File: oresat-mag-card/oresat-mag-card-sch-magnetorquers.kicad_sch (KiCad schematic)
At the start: 79 parts, among them U12 STSPIN250, U13 STSPIN250, U14 INA185, U15 INA185, U16 STSPIN250, U17 INA185

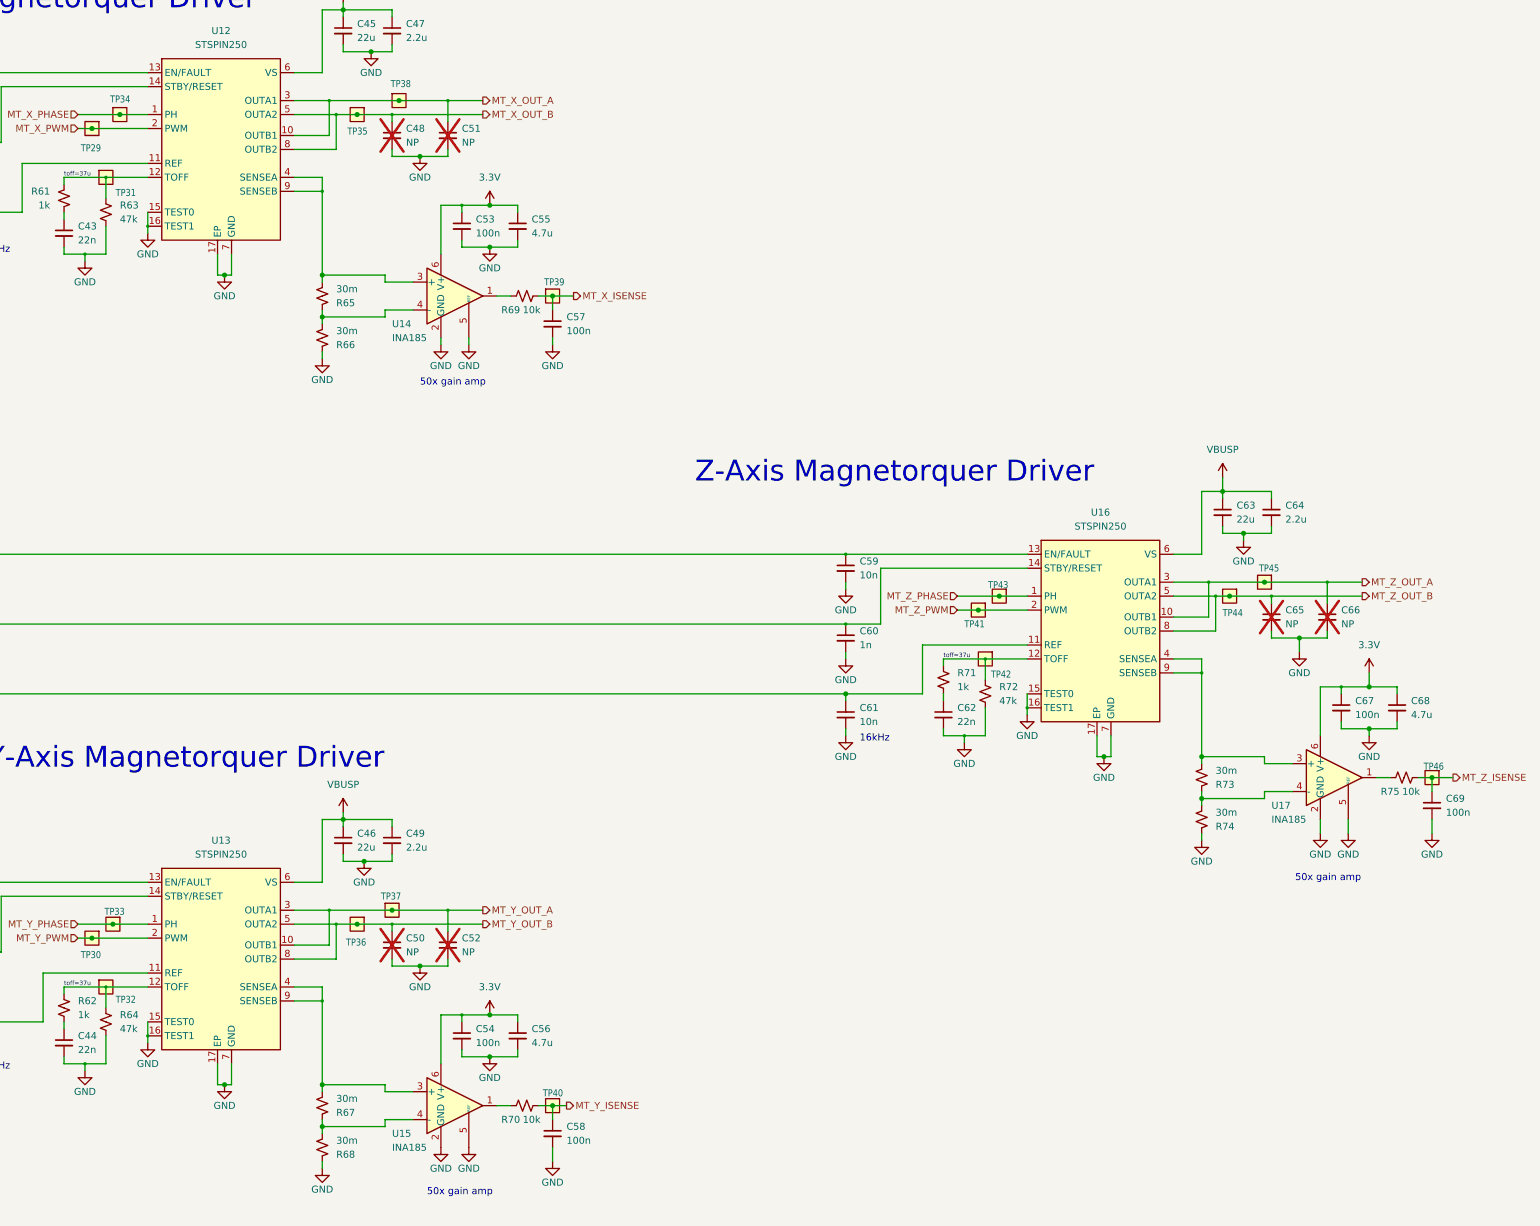
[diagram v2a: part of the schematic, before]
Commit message: Moved to independent MT connectors using pico EZ connectors, and re-laid out the STSPIN250s to be more best-practices.
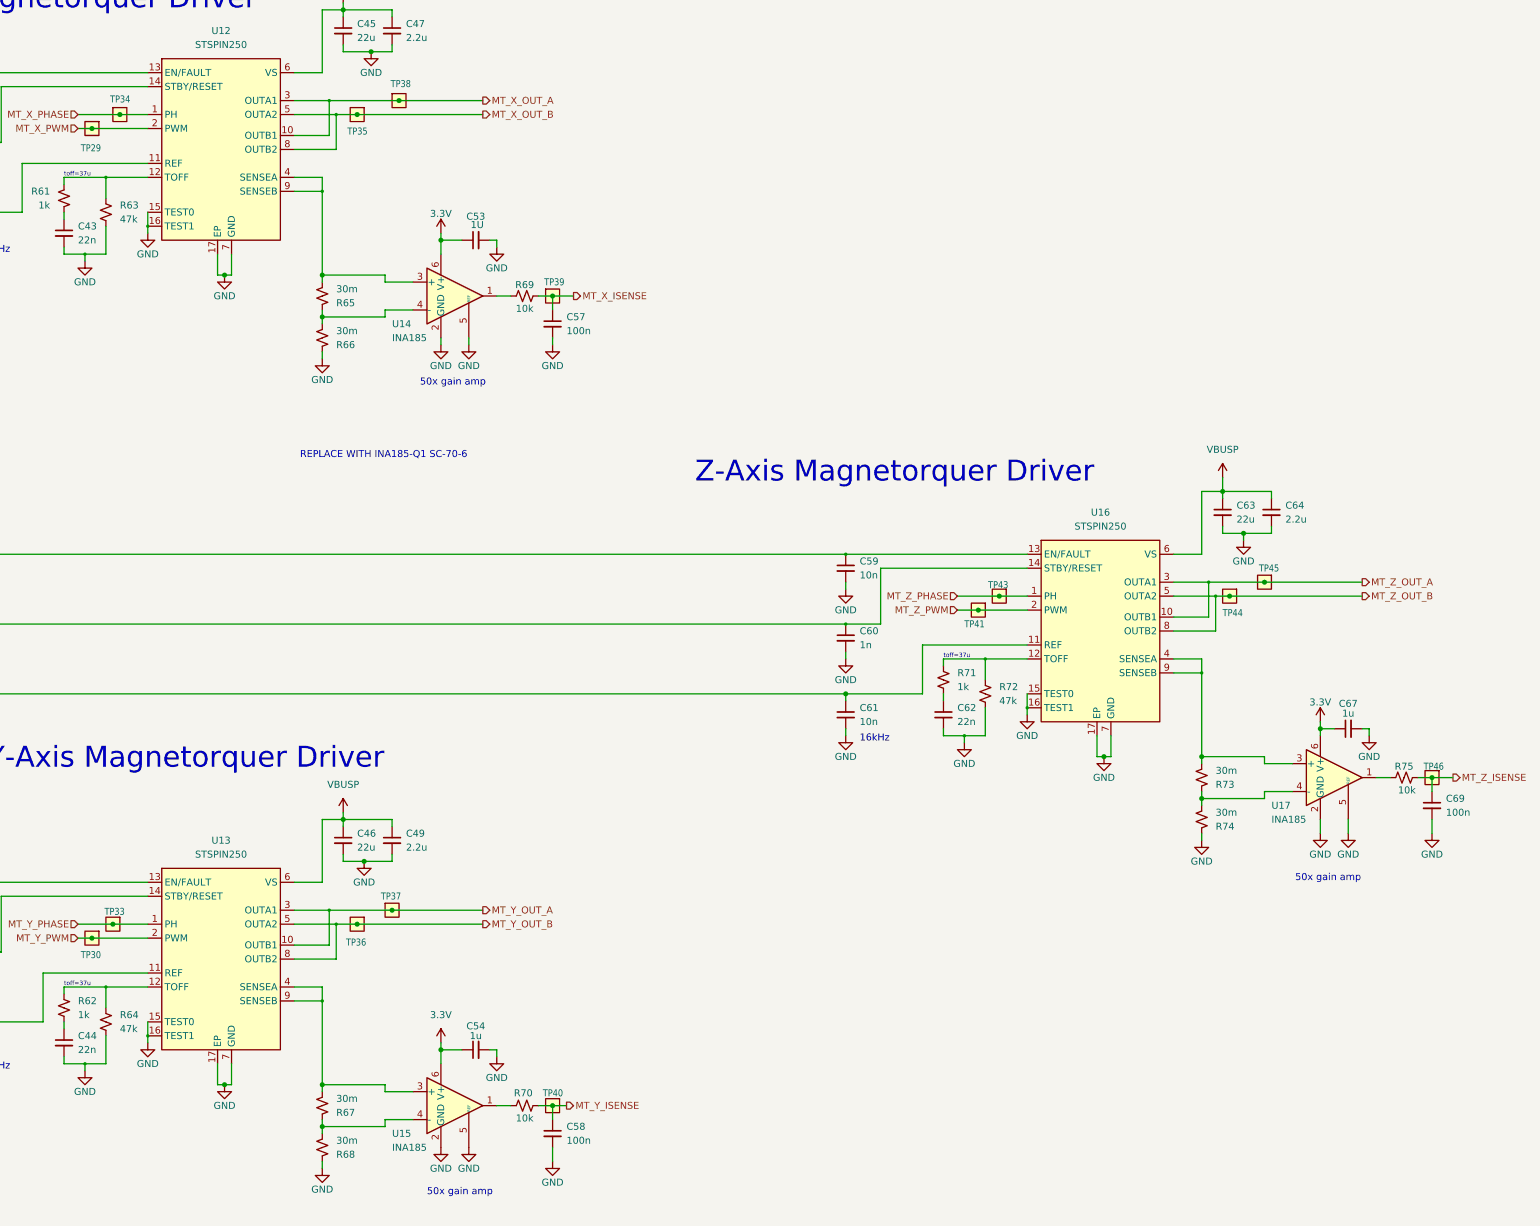
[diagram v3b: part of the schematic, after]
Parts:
- removed C48, C50, C51, C52, C65, C66: NP, oresat-passives:0603-C-NOSILK, symbol Device:C_Small
- removed C55, C56, C68: 4.7u, oresat-passives:0603-C-NOSILK, symbol Device:C_Small
- removed TP31, TP32, TP42: Test-Point, oresat-misc:TestPoint-0.75mm-th, symbol oresat-misc:Test-Point-0.75mm-th
- C37, C39, C40, C42, C59, C61: DIST (none) -> DigiKey; DPN (none) -> 399-12983-1-ND; MFR (none) -> KEMET; MPN (none) -> C0603C103J5RACAUTO
- C38, C41, C60: DIST (none) -> DigiKey; DPN (none) -> 399-12989-1-ND; MFR (none) -> KEMET; MPN (none) -> C0603C102J5RACAUTO
- C47, C49, C64: DIST (none) -> DigiKey; DPN (none) -> 490-GRT188C71E225KE13DCT-ND; MFR (none) -> Murata Electronics; MPN (none) -> GRT188C71E225KE13D
- C53: value 100n -> 1U; DIST (none) -> DigiKey; MFR (none) -> KEMET
- C54, C67: value 100n -> 1u; DIST (none) -> DigiKey; MFR (none) -> KEMET
- C57, C58, C69: DIST (none) -> DigiKey; DPN (none) -> 399-6856-1-ND; MFR (none) -> KEMET; MPN (none) -> C0603C104K5RACAUTO
- R57, R69, R70, R75: DIST (none) -> DigiKey; DPN (none) -> RMCF0603FT10K0CT-ND; MFR (none) -> Stackpole Electronics; MPN (none) -> RMCF0603FT10K0
- R59, R61, R62, R71: DIST (none) -> DigiKey; DPN (none) -> RMCF0603FT2K70CT-ND; MFR (none) -> Stackpole Electronics; MPN (none) -> RMCF0603FT1K00
- R63, R64, R72: DIST (none) -> DigiKey; DPN (none) -> RMCF0603FT47K0CT-ND; MFR (none) -> Stackpole Electronics; MPN (none) -> RMCF0603FT47K0
- R65, R66, R67, R68, R73, R74: DIST (none) -> DigiKey; DPN (none) -> CSR1206FK30L0CT-ND; MFR (none) -> Stackpole Electronics; MPN (none) -> CSR1206FK30L0
- U12, U13, U16: DIST (none) -> DigiKey; DPN (none) -> 497-17035-1-ND; MFR (none) -> STMicroelectronics; MPN (none) -> STSPIN250
- U14, U15, U17: DIST (none) -> DigiKey; DPN (none) -> 296-INA185A2QDCKRQ1CT-ND; MFR (none) -> Texas Instruments; MPN (none) -> INA185A2QDCKRQ1
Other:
- note added: "REPLACE WITH INA185-Q1 SC-70-6"
- moved on the sheet: C53, C54, C67

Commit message: Final mag card
Lots of polishing around best practices layout. Put in giant hole to thread the MTs from below if required for the 3U CubeSats. Cleaned up power layer, added stitching vias, updated readme.
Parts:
- C37, C38, C39, C40, C41, C42, C47, C49, C53, C54, C57, C58, C59, C60, C61, C64, C67, C69, R57, R59, R61, R62, R63, R64, R65, R66, R67, R68, R69, R70, R71, R72, R73, R74, R75, U12, U13, U14, U15, U16, U17: DIS (none) -> DigiKey; DIST DigiKey -> (none)
- C45, C46, C63: DIS (none) -> DigiKey

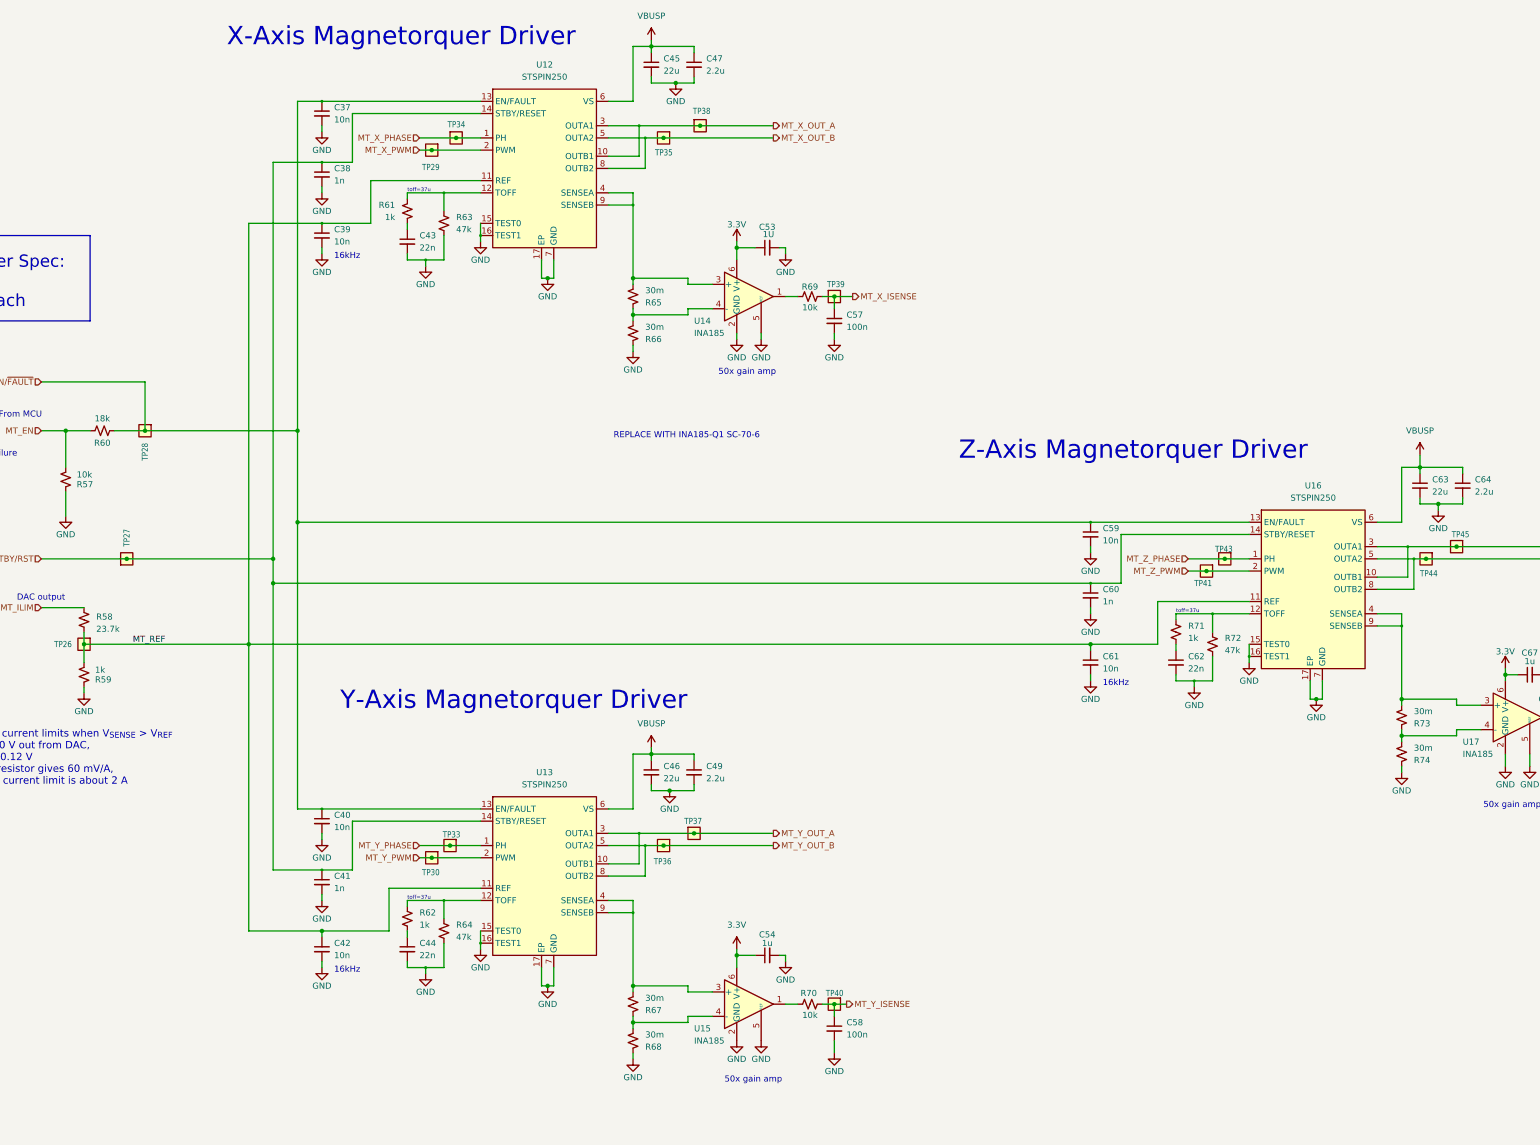
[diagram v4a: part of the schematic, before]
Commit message: Upgraded to kiCad 10, updated BOM during fabrication woes with Colorodo PCBA, no change in PCB
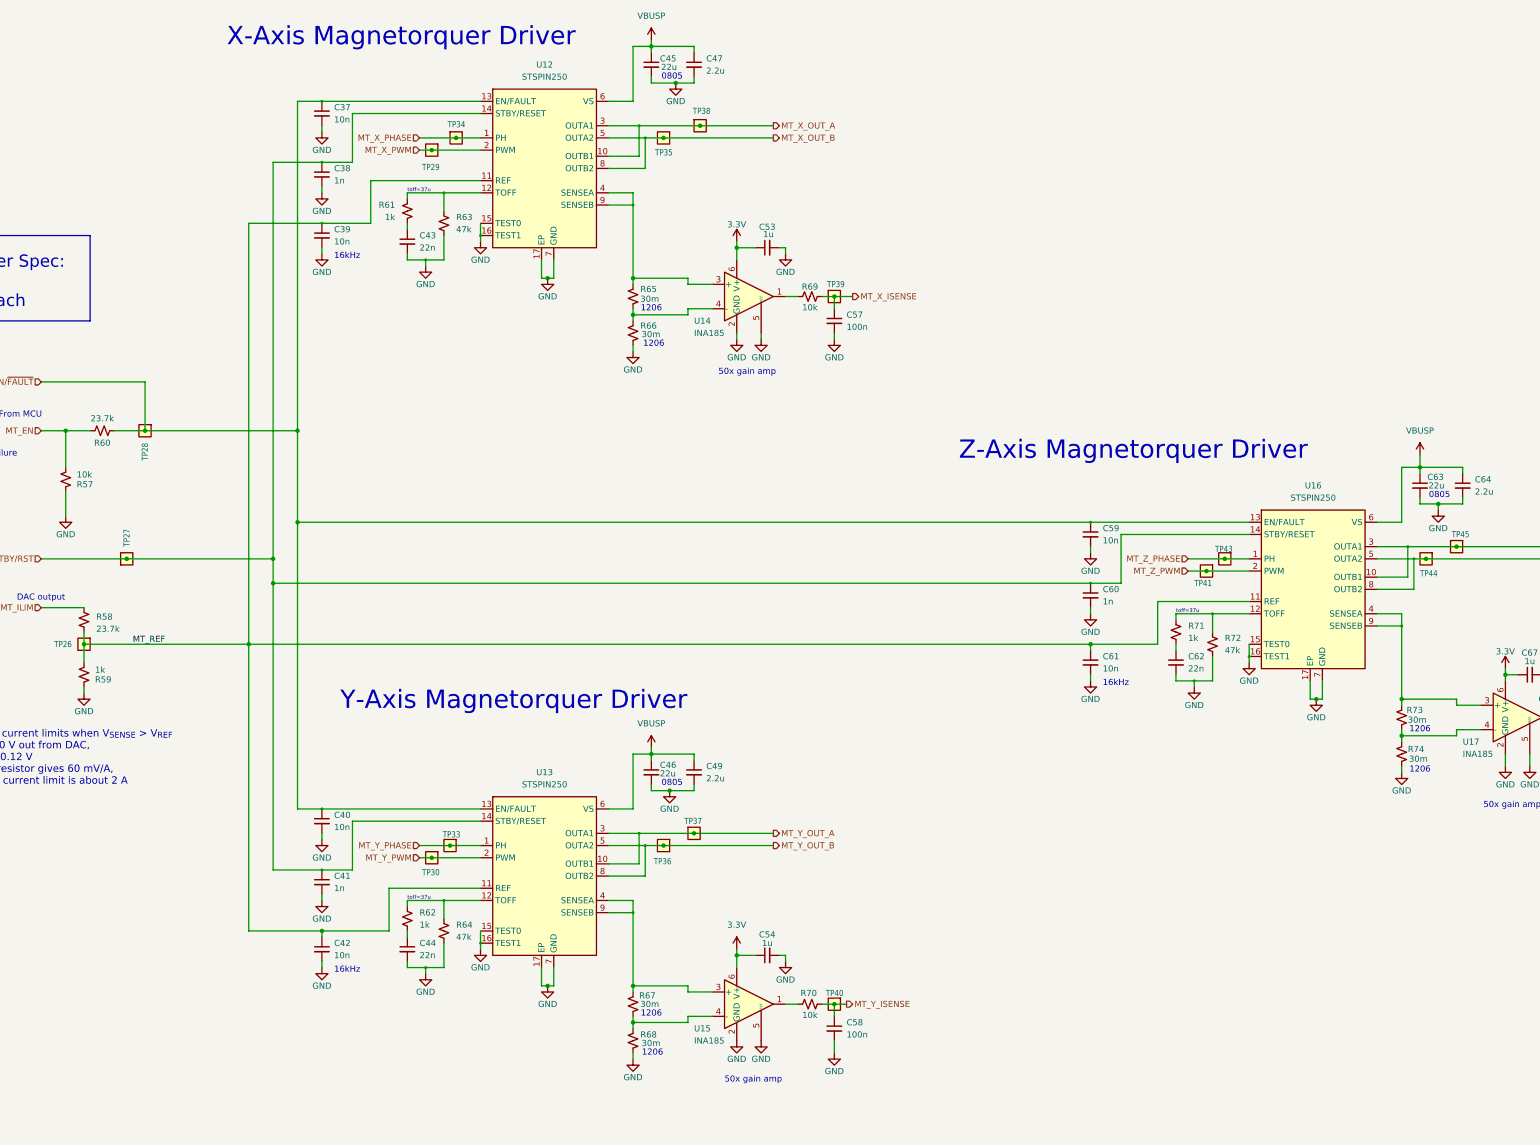
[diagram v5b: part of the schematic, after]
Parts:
- C37, C38, C39, C40, C41, C42, C47, C49, C57, C58, C59, C60, C61, C64, C69, R57, R63, R64, R65, R66, R67, R68, R69, R70, R72, R73, R74, R75, U12, U13, U16: DIST (none) -> DigiKey
- C43, C44, C62: DIST (none) -> DigiKey; DPN (none) -> 399-C0603C223J5RACAUTOCT-ND; MFR (none) -> KEMET; MPN (none) -> C0603C223J5RACAUTO
- C45, C46, C63: DIST (none) -> DigiKey; DPN (none) -> 490-GRT21BC81C226ME13LCT-ND; MFR (none) -> Murata Electronics; MPN (none) -> GRT21BC81C226ME13L
- C53: value 1U -> 1u; DIST (none) -> DigiKey; DPN (none) -> 490-GRT188R71E105KE13DCT-ND; MFR KEMET -> Murata Electronics; MPN (none) -> GRT188R71E105KE13D
- C54, C67: DIST (none) -> DigiKey; DPN (none) -> 490-GRT188R71E105KE13DCT-ND; MFR KEMET -> Murata Electronics; MPN (none) -> GRT188R71E105KE13D
- R58: DIST (none) -> DigiKey; DPN (none) -> RMCF0603FT237RCT-ND; MFR (none) -> Stackpole Electronics Inc; MPN (none) -> RMCF0603FT237R
- R59, R61, R62, R71: DIST (none) -> DigiKey; DPN RMCF0603FT2K70CT-ND -> RMCF0603FT1K00CT-ND
- R60: value 18k -> 23.7k; DIST (none) -> DigiKey; DPN (none) -> RMCF0603FT237RCT-ND; MFR (none) -> Stackpole Electronics Inc; MPN (none) -> RMCF0603FT237R
- U14, U15, U17: DIST (none) -> DigiKey; DPN 296-INA185A2QDCKRQ1CT-ND -> 296-INA185A2IDRLRCT-ND; MPN INA185A2QDCKRQ1 -> INA185A2IDRLR
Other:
- note added: "0805"
- note added: "1206"
- note removed: "REPLACE WITH INA185-Q1 SC-70-6"
